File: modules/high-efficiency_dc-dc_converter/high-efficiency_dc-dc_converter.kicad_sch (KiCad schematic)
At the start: 13 parts

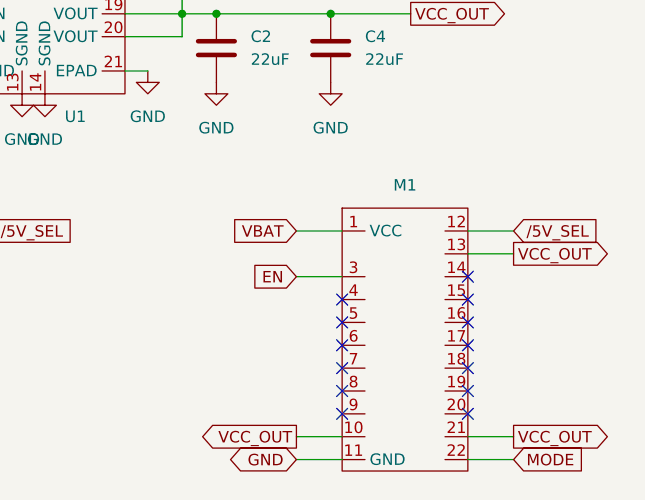
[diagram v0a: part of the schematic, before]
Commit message: update dc-dc converter footprint
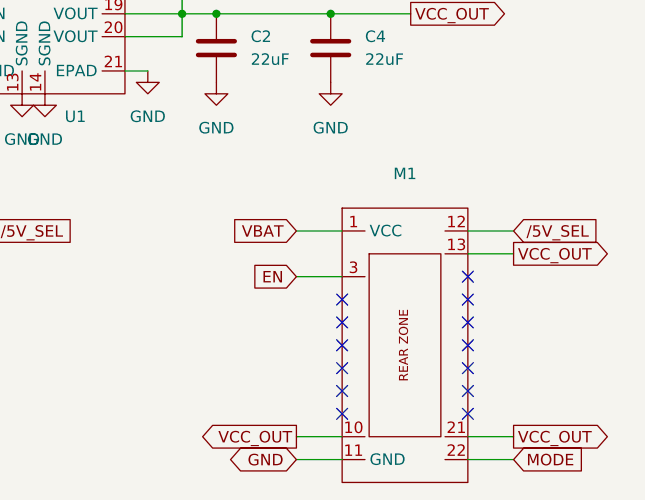
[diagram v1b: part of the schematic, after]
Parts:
- removed M1: ~, MegaCastle:MegaCastle2x11Wide-Module-I13.2x22.25-KA0780C, symbol MegaCastle:MegaCastle2x11-Module
- added M1: ~, MegaCastle:MegaCastle2x11-Module-I15.7x23.1-MA0780C-PANEL-NIBBLE, symbol MegaCastle:MegaCastle2x11-Module-I15.7x23.1-MA0780C
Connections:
- net +4V: now also M1.1 (VCC)
- net EN: now also M1.3
- net GND: now also M1.11 (GND)
- net MODE: now also M1.22
- net VCC_OUT: now also M1.10, M1.13, M1.21
- net /5V_SEL: now also M1.12
